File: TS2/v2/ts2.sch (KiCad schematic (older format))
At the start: 0 parts

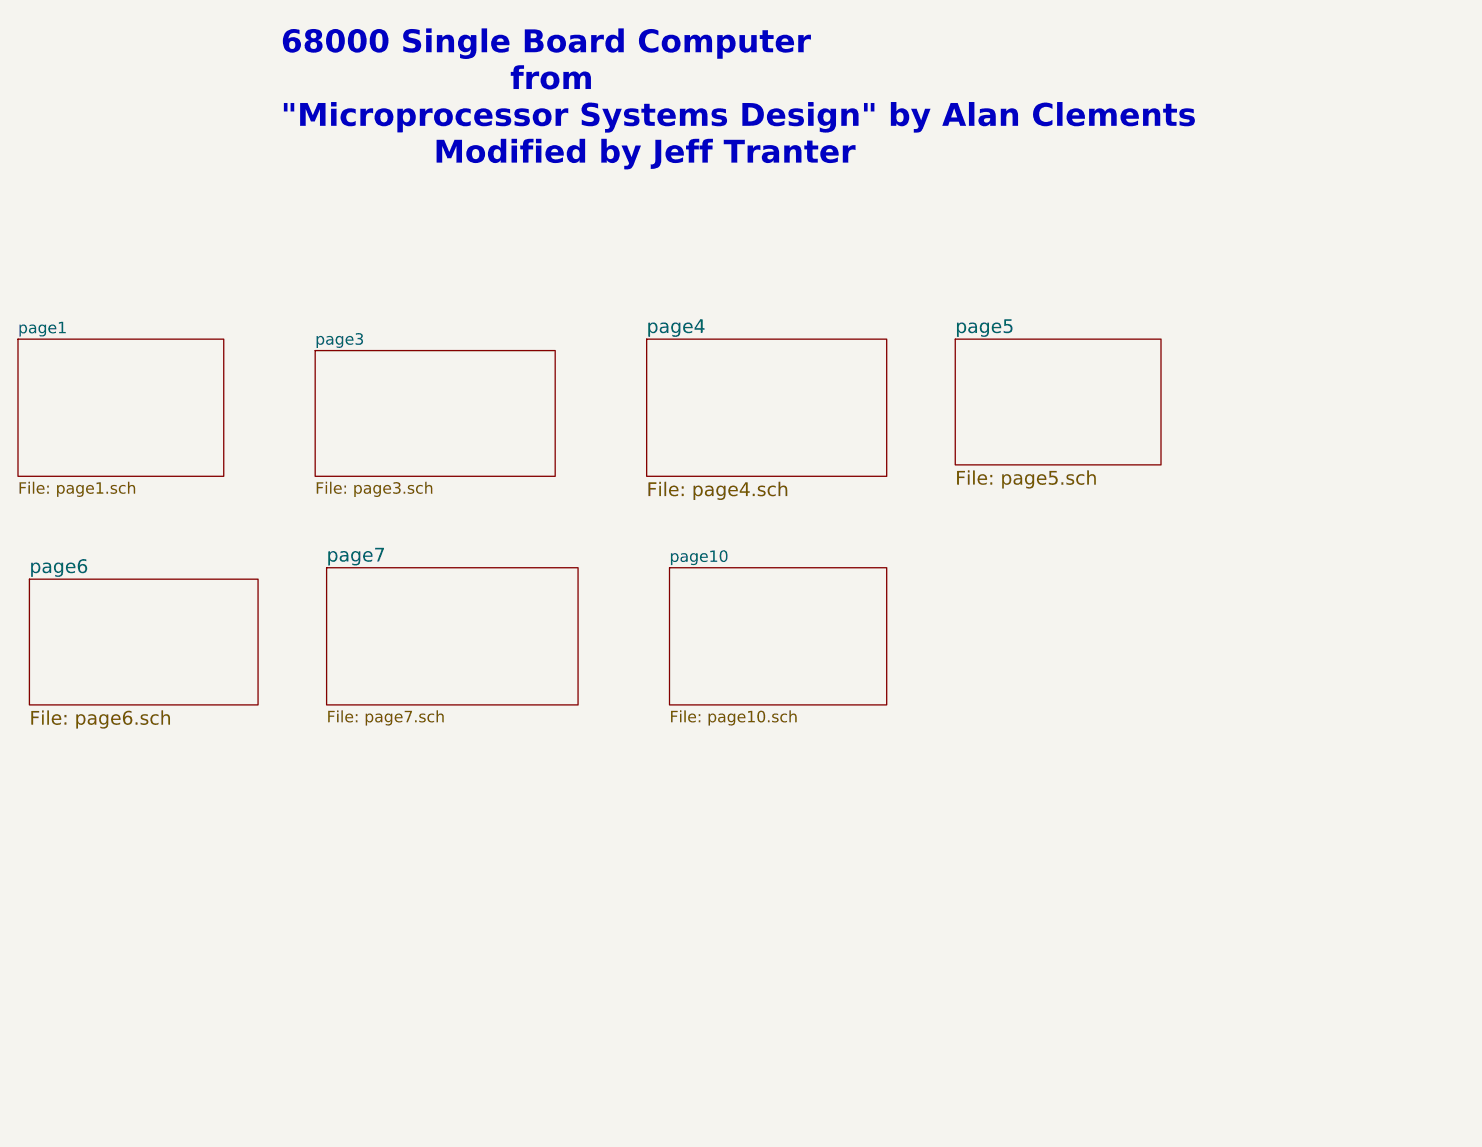
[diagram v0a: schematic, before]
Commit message: Remove extra pages and renumber.
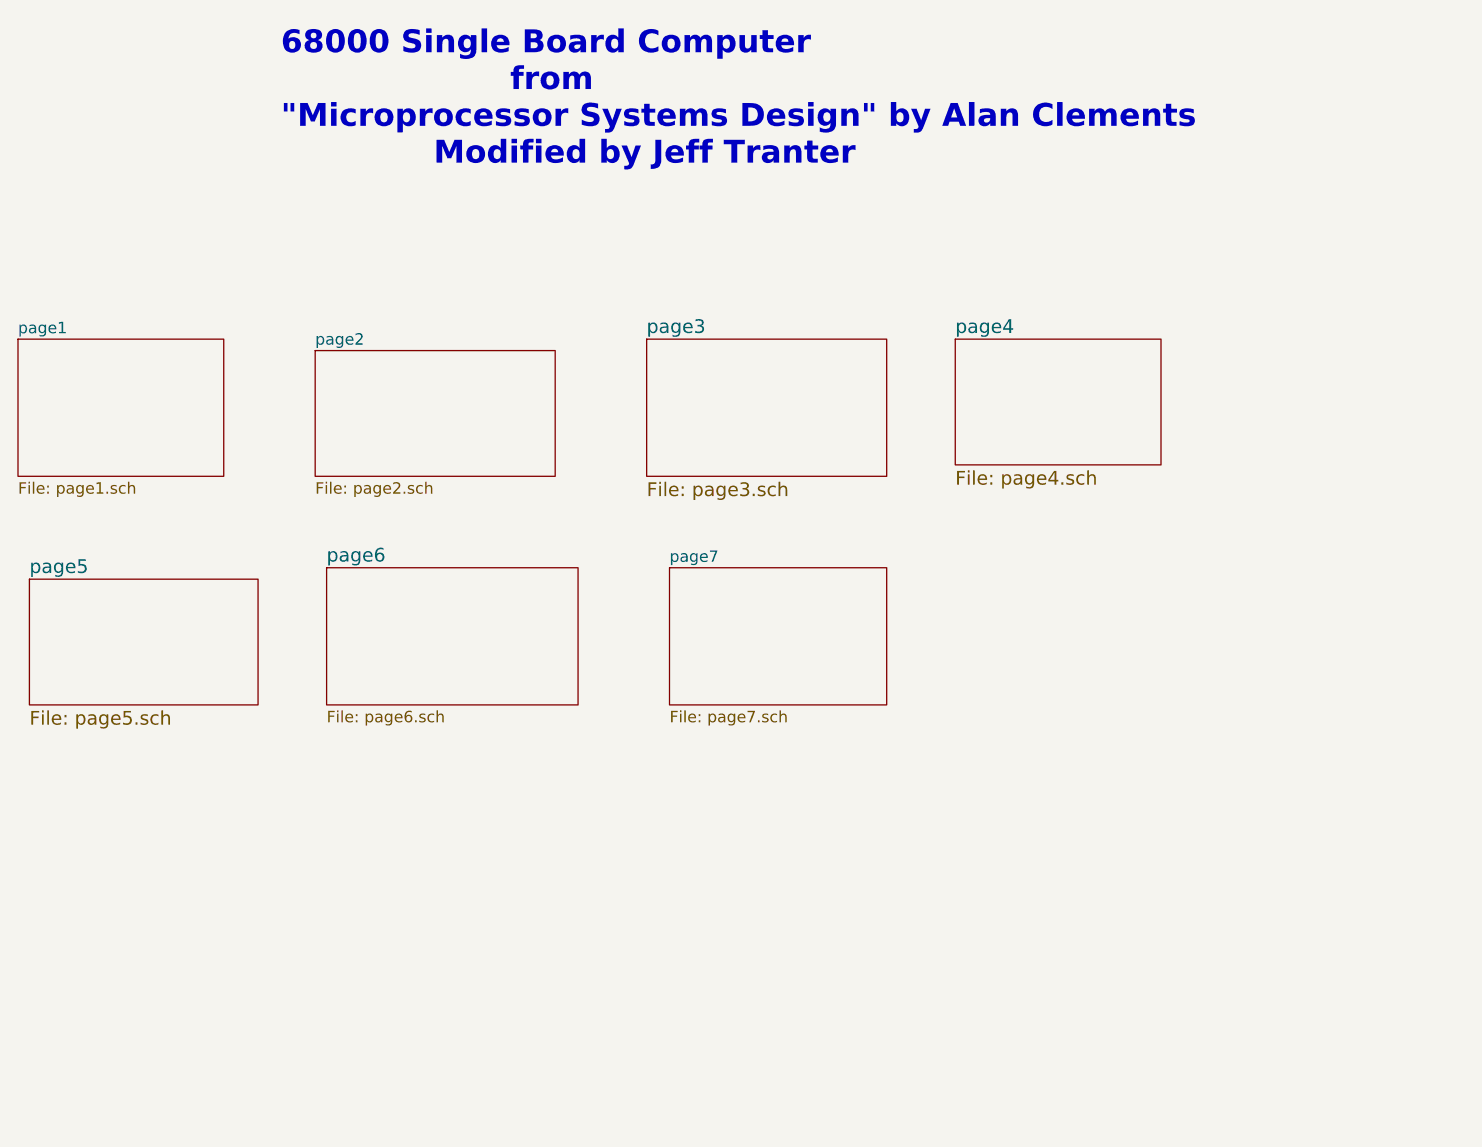
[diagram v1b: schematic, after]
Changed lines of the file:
@@
 S 3400 2250 1050 550
 U 57B64777
-F0 "page3" 50
-F1 "page3.sch" 50
+F0 "page2" 50
+F1 "page2.sch" 50
 $EndSheet
 $Sheet
 S 4850 2200 1050 600
 U 57C2F822
+F0 "page3" 60
+F1 "page3.sch" 60
+$EndSheet
+$Sheet
+S 6200 2200 900  550
+U 57C3779E
 F0 "page4" 60
 F1 "page4.sch" 60
 $EndSheet
 $Sheet
-S 6200 2200 900  550
-U 57C3779E
+S 2150 3250 1000 550
+U 57C4CE2D
 F0 "page5" 60
 F1 "page5.sch" 60
 $EndSheet
 $Sheet
-S 2150 3250 1000 550
-U 57C4CE2D
-F0 "page6" 60
-F1 "page6.sch" 60
-$EndSheet
-$Sheet
 S 3450 3200 1100 600
 U 57C4D163
-F0 "page7" 60
-F1 "page7.sch" 50
+F0 "page6" 60
+F1 "page6.sch" 50
 $EndSheet
 $Sheet
 S 4950 3200 950  600
 U 57C65407
-F0 "page10" 50
-F1 "page10.sch" 50
+F0 "page7" 50
+F1 "page7.sch" 50
 $EndSheet
 Text Notes 3250 1450 0    100  ~ 20

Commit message: more fixup of deleted pages.
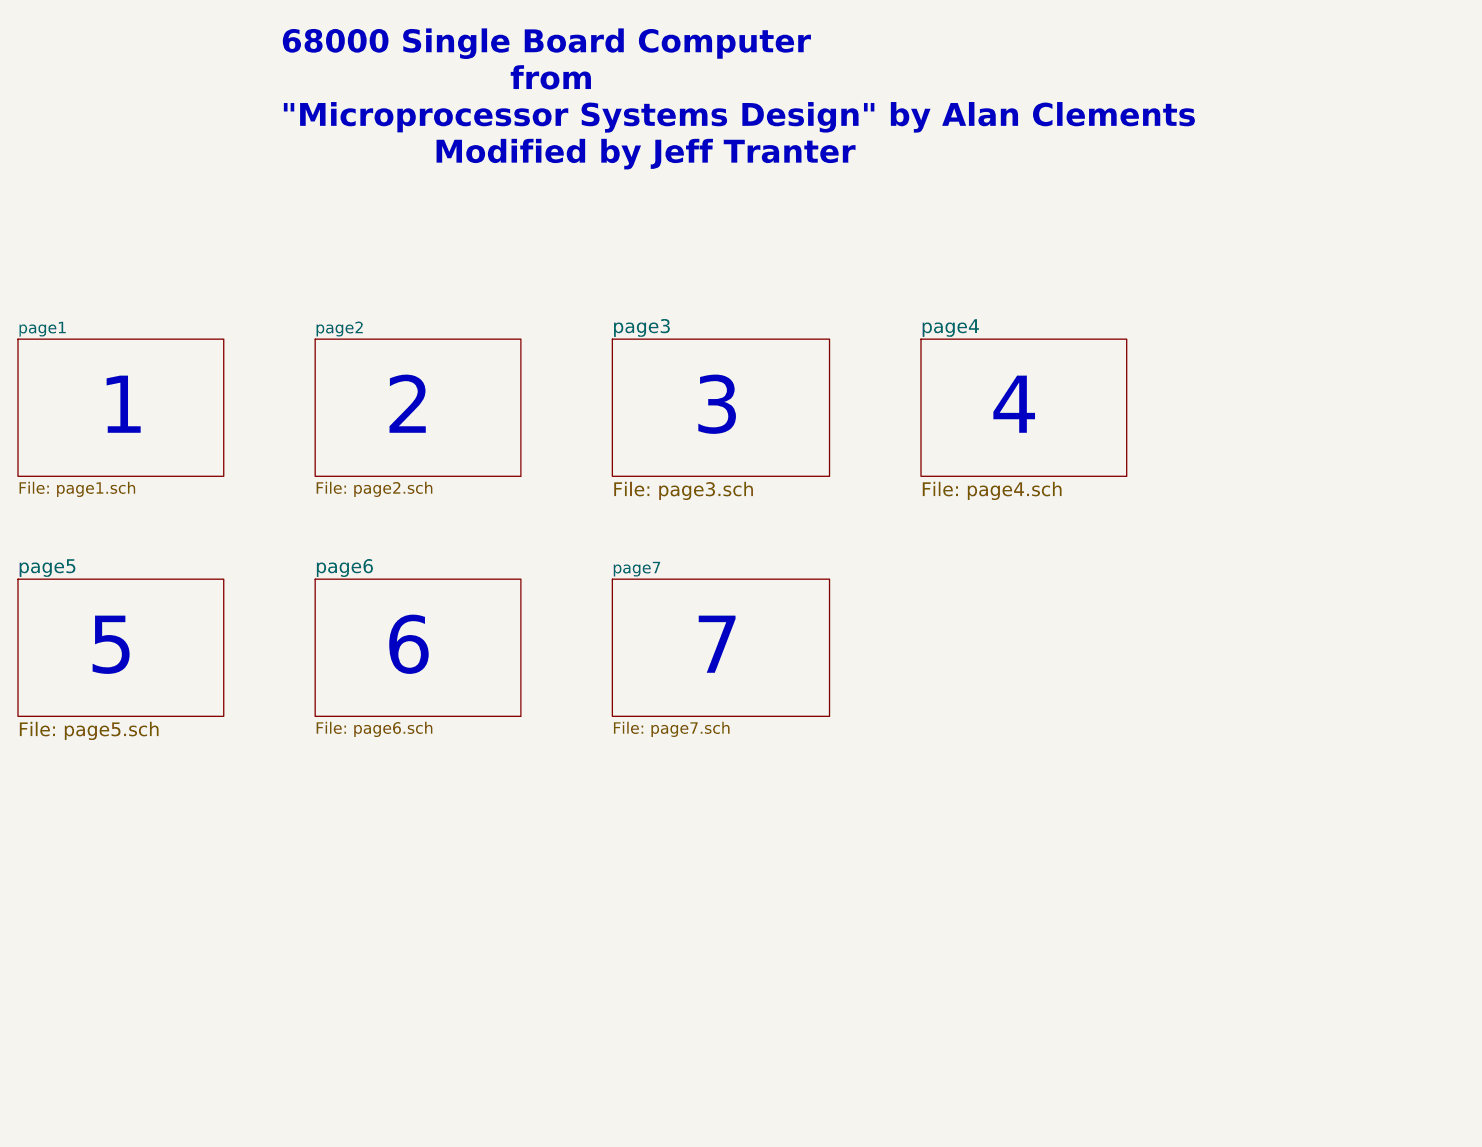
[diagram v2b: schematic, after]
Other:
- note added: "1"
- note added: "2"
- note added: "3"
- note added: "4"
- note added: "5"
- note added: "6"
- note added: "7"
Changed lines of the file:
@@
 $EndSheet
 $Sheet
-S 3400 2250 1050 550
+S 3400 2200 900  600
 U 57B64777
 F0 "page2" 50
@@
 $EndSheet
 $Sheet
-S 4850 2200 1050 600
+S 4700 2200 950  600
 U 57C2F822
 F0 "page3" 60
@@
 $EndSheet
 $Sheet
-S 6200 2200 900  550
+S 6050 2200 900  600
 U 57C3779E
 F0 "page4" 60
@@
 $EndSheet
 $Sheet
-S 2150 3250 1000 550
+S 2100 3250 900  600
 U 57C4CE2D
 F0 "page5" 60
@@
 $EndSheet
 $Sheet
-S 3450 3200 1100 600
+S 3400 3250 900  600
 U 57C4D163
 F0 "page6" 60
 F1 "page6.sch" 50
 $EndSheet
+Text Notes 3250 1450 0    100  ~ 20
+             68000 Single Board Computer\n                     from\n"Microprocessor Systems Design" by Alan Clements\n              Modified by Jeff Tranter
+Text Notes 5050 3700 0    250  ~ 0
+7
+Text Notes 3700 3700 0    250  ~ 0
+6
+Text Notes 2400 3700 0    250  ~ 0
+5
+Text Notes 6350 2650 0    250  ~ 0
+4
+Text Notes 5050 2650 0    250  ~ 0
+3
+Text Notes 3700 2650 0    250  ~ 0
+2
+Text Notes 2450 2650 0    250  ~ 0
+1
 $Sheet
-S 4950 3200 950  600
+S 4700 3250 950  600
 U 57C65407
 F0 "page7" 50
 F1 "page7.sch" 50
 $EndSheet
-Text Notes 3250 1450 0    100  ~ 20
-             68000 Single Board Computer\n                     from\n"Microprocessor Systems Design" by Alan Clements\n              Modified by Jeff Tranter
 $EndSCHEMATC

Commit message: Updates, add PDF and BOM.
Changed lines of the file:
@@
 Date "2016-09-03"
 Rev "2.0"
-Comp ""
+Comp "Jeff Tranter"
 Comment1 "Top Level Schematic"
 Comment2 ""
@@
 F1 "page7.sch" 50
 $EndSheet
+$Comp
+L VCC #PWR01
+U 1 1 57CB9891
+P 2400 4750
+F 0 "#PWR01" H 2400 4600 50  0001 C CNN
+F 1 "VCC" H 2400 4900 50  0000 C CNN
+F 2 "" H 2400 4750 50  0000 C CNN
+F 3 "" H 2400 4750 50  0000 C CNN
+	1    2400 4750
+	1    0    0    -1
+$EndComp
+$Comp
+L GND #PWR02
+U 1 1 57CB98A5
+P 2400 5400
+F 0 "#PWR02" H 2400 5150 50  0001 C CNN
+F 1 "GND" H 2400 5250 50  0000 C CNN
+F 2 "" H 2400 5400 50  0000 C CNN
+F 3 "" H 2400 5400 50  0000 C CNN
+	1    2400 5400
+	1    0    0    -1
+$EndComp
+$Comp
+L PWR_FLAG #FLG03
+U 1 1 57CBBC87
+P 2400 4750
+F 0 "#FLG03" H 2400 4845 50  0001 C CNN
+F 1 "PWR_FLAG" H 2400 4930 50  0000 C CNN
+F 2 "" H 2400 4750 50  0000 C CNN
+F 3 "" H 2400 4750 50  0000 C CNN
+	1    2400 4750
+	-1   0    0    1
+$EndComp
+$Comp
+L PWR_FLAG #FLG04
+U 1 1 57CBBFC3
+P 2400 5400
+F 0 "#FLG04" H 2400 5495 50  0001 C CNN
+F 1 "PWR_FLAG" H 2400 5580 50  0000 C CNN
+F 2 "" H 2400 5400 50  0000 C CNN
+F 3 "" H 2400 5400 50  0000 C CNN
+	1    2400 5400
+	1    0    0    -1
+$EndComp
 $EndSCHEMATC

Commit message: Small updates.
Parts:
- added C4: 100uF, symbol CP1
- added C5: 0.1uF, symbol C
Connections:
- net GND: now also C4.2, C5.2
- net VCC: now also C4.1, C5.1
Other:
- note added: "One per IC"
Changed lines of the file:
@@
 	1    0    0    -1
 $EndComp
+$Comp
+L CP1 C4
+U 1 1 57D36826
+P 3050 4800
+F 0 "C4" H 3075 4900 50  0000 L CNN
+F 1 "100uF" H 3075 4700 50  0000 L CNN
+F 2 "" H 3050 4800 50  0000 C CNN
+F 3 "" H 3050 4800 50  0000 C CNN
+	1    3050 4800
+	1    0    0    -1
+$EndComp
+$Comp
+L GND #PWR05
+U 1 1 57D36855
+P 3050 4950
+F 0 "#PWR05" H 3050 4700 50  0001 C CNN
+F 1 "GND" H 3050 4800 50  0000 C CNN
+F 2 "" H 3050 4950 50  0000 C CNN
+F 3 "" H 3050 4950 50  0000 C CNN
+	1    3050 4950
+	1    0    0    -1
+$EndComp
+$Comp
+L VCC #PWR06
+U 1 1 57D3686B
+P 3050 4650
+F 0 "#PWR06" H 3050 4500 50  0001 C CNN
+F 1 "VCC" H 3050 4800 50  0000 C CNN
+F 2 "" H 3050 4650 50  0000 C CNN
+F 3 "" H 3050 4650 50  0000 C CNN
+	1    3050 4650
+	1    0    0    -1
+$EndComp
+$Comp
+L C C5
+U 1 1 57D36890
+P 3650 4800
+F 0 "C5" H 3675 4900 50  0000 L CNN
+F 1 "0.1uF" H 3675 4700 50  0000 L CNN
+F 2 "" H 3688 4650 50  0000 C CNN
+F 3 "" H 3650 4800 50  0000 C CNN
+	1    3650 4800
+	1    0    0    -1
+$EndComp
+$Comp
+L GND #PWR07
+U 1 1 57D368BF
+P 3650 4950
+F 0 "#PWR07" H 3650 4700 50  0001 C CNN
+F 1 "GND" H 3650 4800 50  0000 C CNN
+F 2 "" H 3650 4950 50  0000 C CNN
+F 3 "" H 3650 4950 50  0000 C CNN
+	1    3650 4950
+	1    0    0    -1
+$EndComp
+$Comp
+L VCC #PWR08
+U 1 1 57D368D7
+P 3650 4650
+F 0 "#PWR08" H 3650 4500 50  0001 C CNN
+F 1 "VCC" H 3650 4800 50  0000 C CNN
+F 2 "" H 3650 4650 50  0000 C CNN
+F 3 "" H 3650 4650 50  0000 C CNN
+	1    3650 4650
+	1    0    0    -1
+$EndComp
+Text Notes 3450 4400 0    60   ~ 0
+One per IC
 $EndSCHEMATC

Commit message: Minor tweaks
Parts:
- added D2: POWER, symbol LED
- added R25: 330, symbol R
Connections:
- net GND: now also R25.2
- net VCC: now also D2.2 (A)
- new net: D2.1 (K), R25.1
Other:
- note added: "Bypass caps,\none per IC"
- note removed: "One per IC"
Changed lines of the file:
@@
 L VCC #PWR01
 U 1 1 57CB9891
-P 2400 4750
-F 0 "#PWR01" H 2400 4600 50  0001 C CNN
-F 1 "VCC" H 2400 4900 50  0000 C CNN
-F 2 "" H 2400 4750 50  0000 C CNN
-F 3 "" H 2400 4750 50  0000 C CNN
-	1    2400 4750
+P 2400 4650
+F 0 "#PWR01" H 2400 4500 50  0001 C CNN
+F 1 "VCC" H 2400 4800 50  0000 C CNN
+F 2 "" H 2400 4650 50  0000 C CNN
+F 3 "" H 2400 4650 50  0000 C CNN
+	1    2400 4650
 	1    0    0    -1
 $EndComp
@@
 L GND #PWR02
 U 1 1 57CB98A5
-P 2400 5400
-F 0 "#PWR02" H 2400 5150 50  0001 C CNN
-F 1 "GND" H 2400 5250 50  0000 C CNN
-F 2 "" H 2400 5400 50  0000 C CNN
-F 3 "" H 2400 5400 50  0000 C CNN
-	1    2400 5400
+P 2400 5450
+F 0 "#PWR02" H 2400 5200 50  0001 C CNN
+F 1 "GND" H 2400 5300 50  0000 C CNN
+F 2 "" H 2400 5450 50  0000 C CNN
+F 3 "" H 2400 5450 50  0000 C CNN
+	1    2400 5450
 	1    0    0    -1
 $EndComp
@@
 L PWR_FLAG #FLG03
 U 1 1 57CBBC87
-P 2400 4750
-F 0 "#FLG03" H 2400 4845 50  0001 C CNN
-F 1 "PWR_FLAG" H 2400 4930 50  0000 C CNN
-F 2 "" H 2400 4750 50  0000 C CNN
-F 3 "" H 2400 4750 50  0000 C CNN
-	1    2400 4750
+P 2400 4650
+F 0 "#FLG03" H 2400 4745 50  0001 C CNN
+F 1 "PWR_FLAG" H 2400 4830 50  0000 C CNN
+F 2 "" H 2400 4650 50  0000 C CNN
+F 3 "" H 2400 4650 50  0000 C CNN
+	1    2400 4650
 	-1   0    0    1
 $EndComp
@@
 L PWR_FLAG #FLG04
 U 1 1 57CBBFC3
-P 2400 5400
-F 0 "#FLG04" H 2400 5495 50  0001 C CNN
-F 1 "PWR_FLAG" H 2400 5580 50  0000 C CNN
-F 2 "" H 2400 5400 50  0000 C CNN
-F 3 "" H 2400 5400 50  0000 C CNN
-	1    2400 5400
+P 2400 5450
+F 0 "#FLG04" H 2400 5545 50  0001 C CNN
+F 1 "PWR_FLAG" H 2400 5630 50  0000 C CNN
+F 2 "" H 2400 5450 50  0000 C CNN
+F 3 "" H 2400 5450 50  0000 C CNN
+	1    2400 5450
 	1    0    0    -1
 $EndComp
@@
 	1    0    0    -1
 $EndComp
-Text Notes 3450 4400 0    60   ~ 0
-One per IC
+Text Notes 3450 4350 0    60   ~ 0
+Bypass caps,\none per IC
+$Comp
+L LED D2
+U 1 1 57D89DCF
+P 4300 4850
+F 0 "D2" V 4300 4950 50  0000 C CNN
+F 1 "POWER" V 4300 4650 50  0000 C CNN
+F 2 "" H 4300 4850 50  0000 C CNN
+F 3 "" H 4300 4850 50  0000 C CNN
+	1    4300 4850
+	0    -1   -1   0
+$EndComp
+$Comp
+L R R25
+U 1 1 57D89E08
+P 4300 5300
+F 0 "R25" V 4380 5300 50  0000 C CNN
+F 1 "330" V 4300 5300 50  0000 C CNN
+F 2 "" V 4230 5300 50  0000 C CNN
+F 3 "" H 4300 5300 50  0000 C CNN
+	1    4300 5300
+	1    0    0    -1
+$EndComp
+$Comp
+L GND #PWR09
+U 1 1 57D89E43
+P 4300 5450
+F 0 "#PWR09" H 4300 5200 50  0001 C CNN
+F 1 "GND" H 4300 5300 50  0000 C CNN
+F 2 "" H 4300 5450 50  0000 C CNN
+F 3 "" H 4300 5450 50  0000 C CNN
+	1    4300 5450
+	1    0    0    -1
+$EndComp
+$Comp
+L VCC #PWR010
+U 1 1 57D89E5F
+P 4300 4650
+F 0 "#PWR010" H 4300 4500 50  0001 C CNN
+F 1 "VCC" H 4300 4800 50  0000 C CNN
+F 2 "" H 4300 4650 50  0000 C CNN
+F 3 "" H 4300 4650 50  0000 C CNN
+	1    4300 4650
+	1    0    0    -1
+$EndComp
+Wire Wire Line
+	4300 5050 4300 5150
 $EndSCHEMATC
